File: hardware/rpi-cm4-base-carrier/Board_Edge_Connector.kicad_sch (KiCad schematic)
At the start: 3 parts, among them J2 ERM8-040-01-X-D-EM2-L-XX, J8 Conn_02x10_Odd_Even, U2 74LVC1G07SE-7

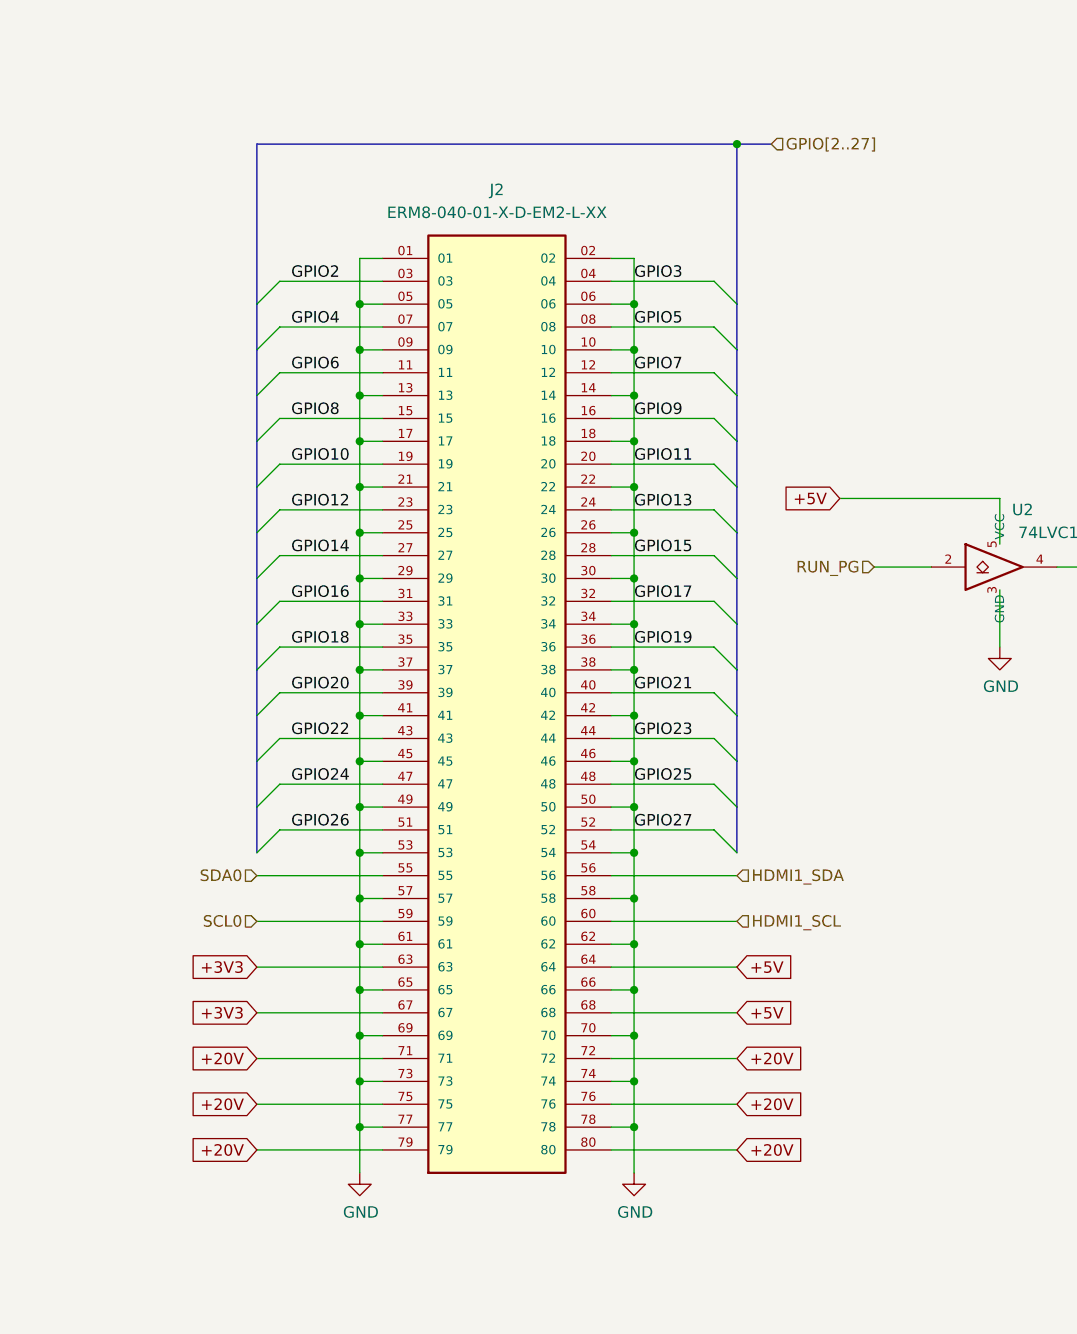
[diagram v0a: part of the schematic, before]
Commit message: board edge connector mostly connected
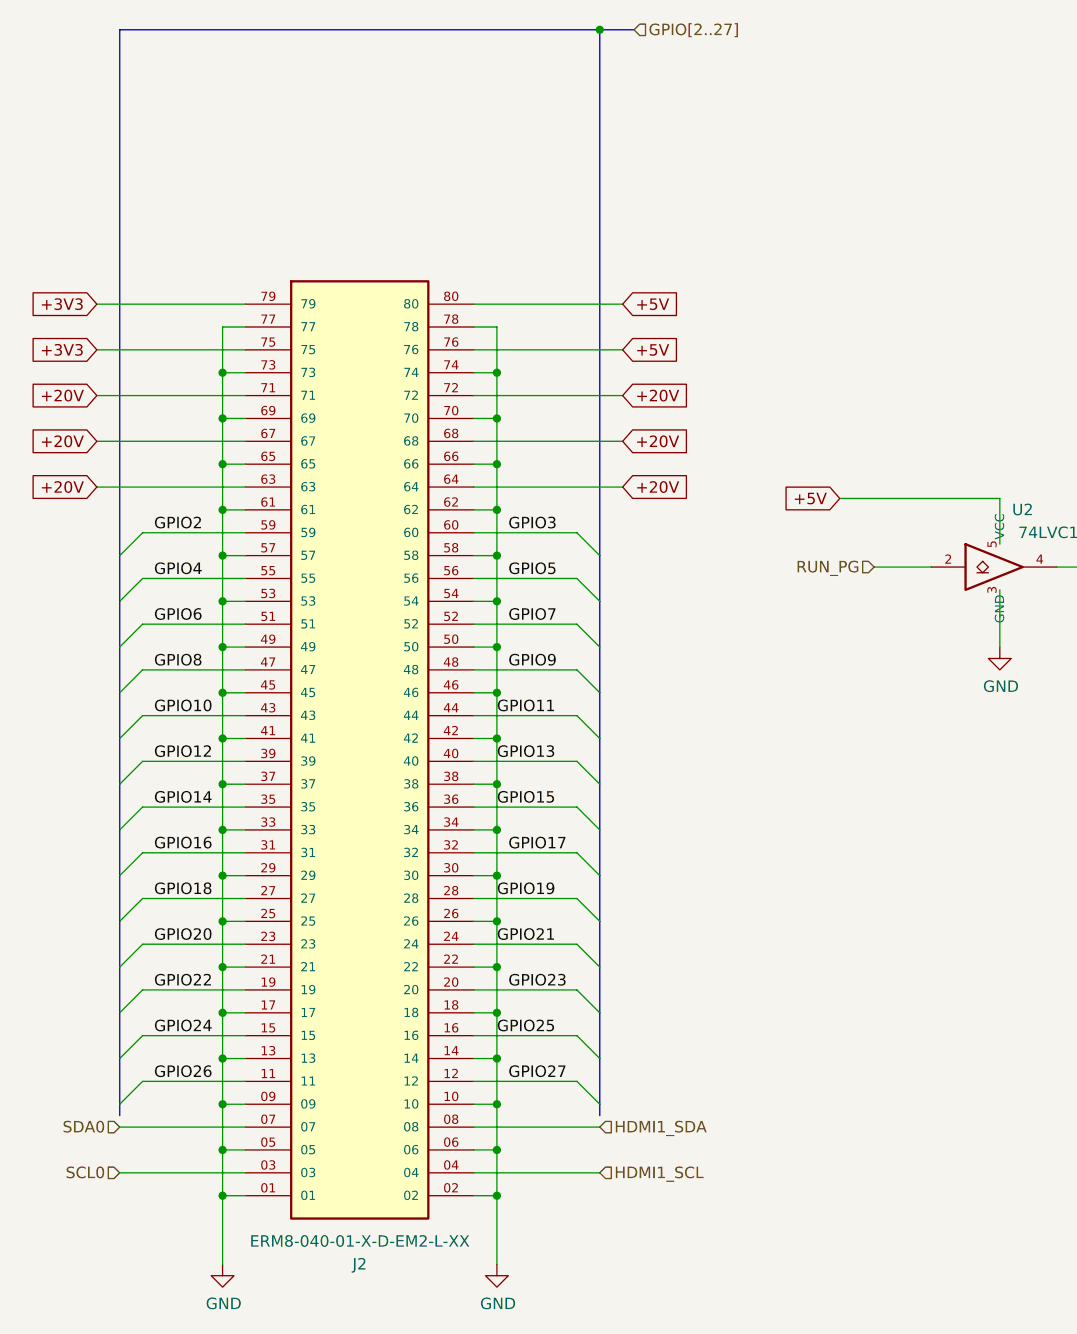
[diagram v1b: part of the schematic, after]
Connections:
- net +20V: now also J2.63, J2.64, J2.67, J2.68; no longer J2.75, J2.76, J2.79, J2.80
- net +3V3: now also J2.75, J2.79; no longer J2.63, J2.67
- net +5V: now also J2.76, J2.80; no longer J2.64, J2.68
- net GND: no longer J2.04, J2.08, J2.12, J2.20, J2.32, J2.48, J2.52, J8.1 (Pin_1), J8.2 (Pin_2)
- net GPIO10: now also J2.43; no longer J2.19
- net GPIO12: now also J2.39; no longer J2.23
- net GPIO14: now also J2.35; no longer J2.27
- net GPIO18: now also J2.27; no longer J2.35
- net GPIO2: now also J2.59; no longer J2.03
- net GPIO20: now also J2.23; no longer J2.39
- net GPIO22: now also J2.19; no longer J2.43
- net GPIO24: now also J2.15; no longer J2.47
- net GPIO26: now also J2.11; no longer J2.51
- net GPIO4: now also J2.55; no longer J2.07
- net GPIO6: now also J2.51; no longer J2.11
- net GPIO8: now also J2.47; no longer J2.15
- net HDMI1_SCL: now also J2.04; no longer J2.60
- net HDMI1_SDA: now also J2.08; no longer J2.56
- net SCL0: now also J2.03; no longer J2.59
- net SDA0: now also J2.07; no longer J2.55
- new net GPIO17: J2.32
- new net GPIO23: J2.20
- new net GPIO27: J2.12
- new net GPIO3: J2.60
- new net GPIO5: J2.56
- new net GPIO7: J2.52, J8.2 (Pin_2)
- new net GPIO9: J2.48, J8.1 (Pin_1)

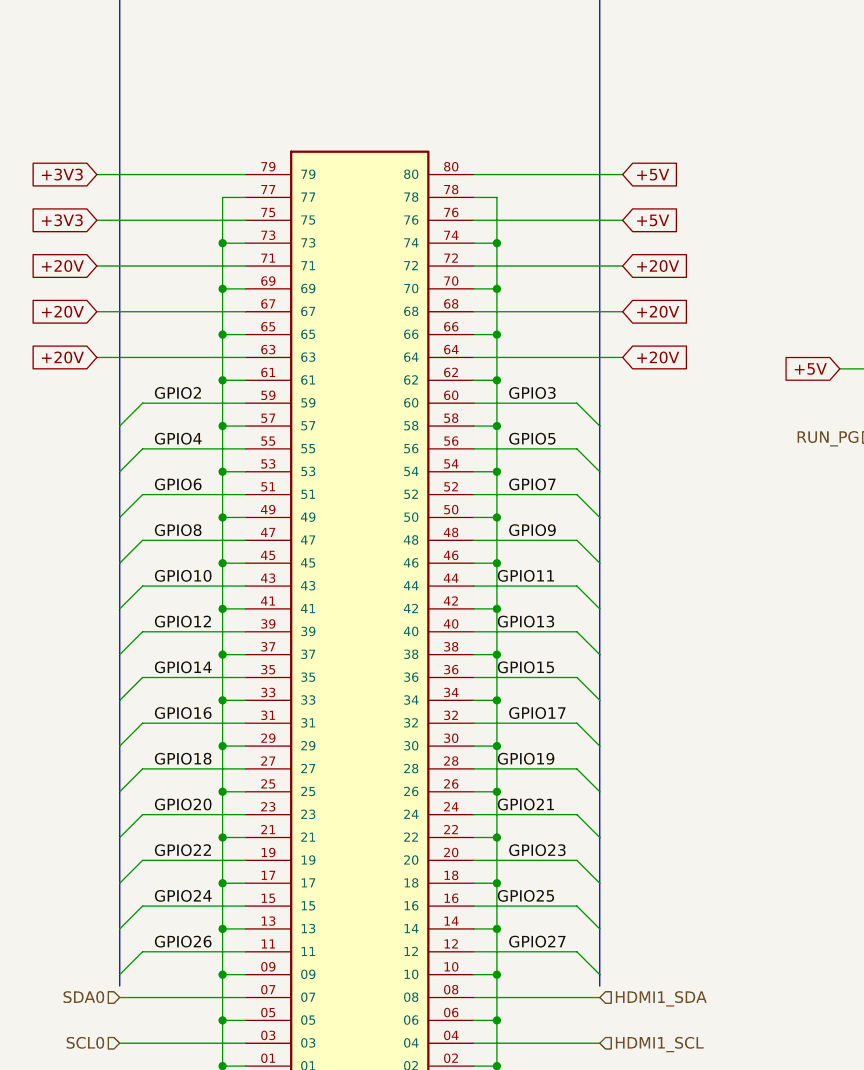
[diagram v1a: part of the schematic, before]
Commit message: good routing and power plane progress, just some final plane progress remaining
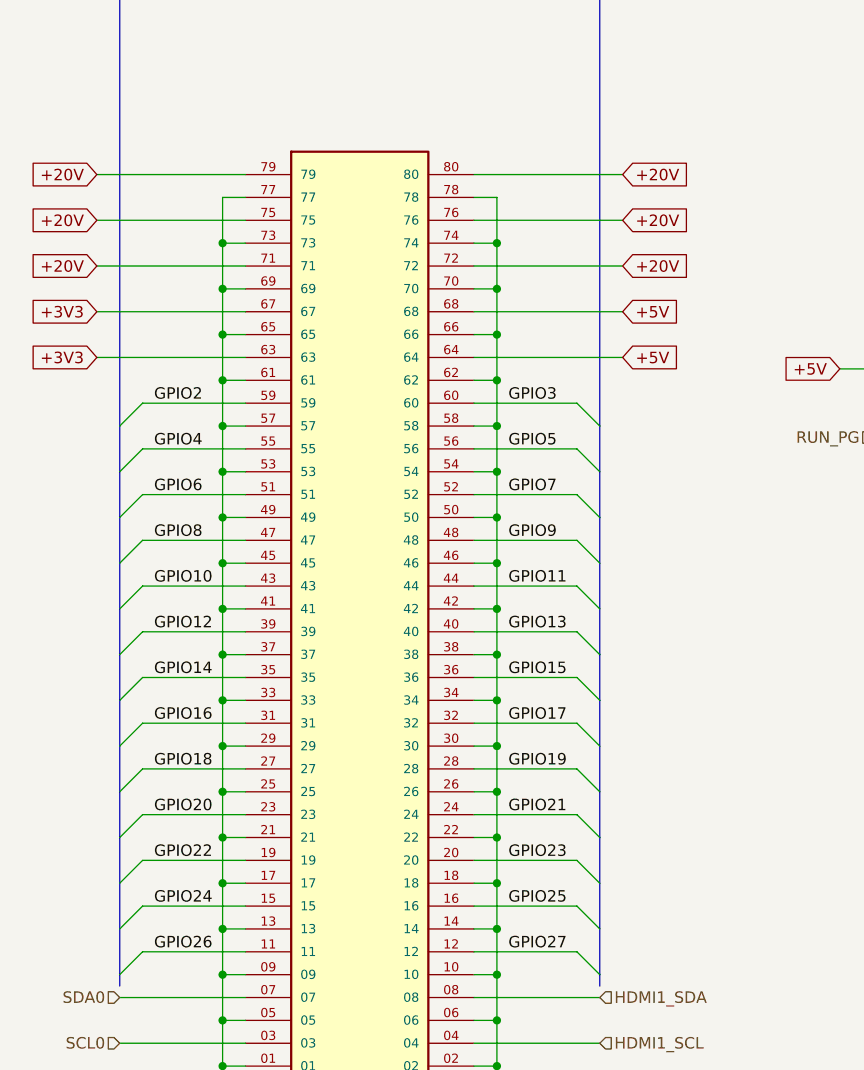
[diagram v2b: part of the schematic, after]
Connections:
- net +20V: now also J2.75, J2.76, J2.79, J2.80; no longer J2.63, J2.64, J2.67, J2.68
- net +3V3: now also J2.63, J2.67; no longer J2.75, J2.79
- net +5V: now also J2.64, J2.68; no longer J2.76, J2.80
- net GND: no longer J2.16, J2.24, J2.28, J2.36, J2.40, J2.44, J8.5 (Pin_5), J8.6 (Pin_6)
- new net GPIO11: J2.44, J8.6 (Pin_6)
- new net GPIO13: J2.40
- new net GPIO15: J2.36, J8.5 (Pin_5)
- new net GPIO19: J2.28
- new net GPIO21: J2.24
- new net GPIO25: J2.16

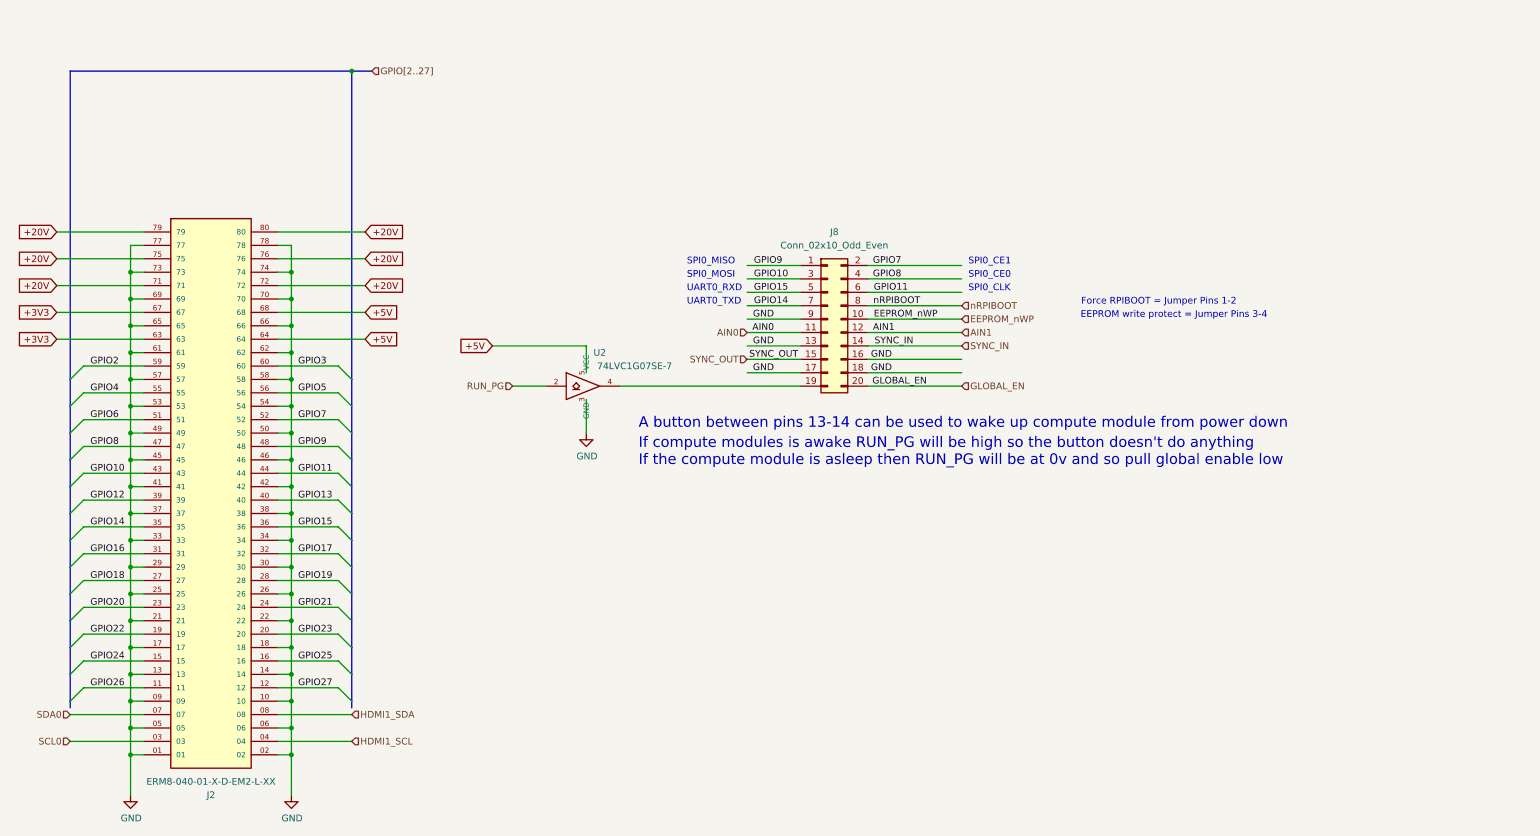
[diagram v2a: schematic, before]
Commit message: convert IC refs to U refs and re-annotate, add fiducials and extra via stitching to layout
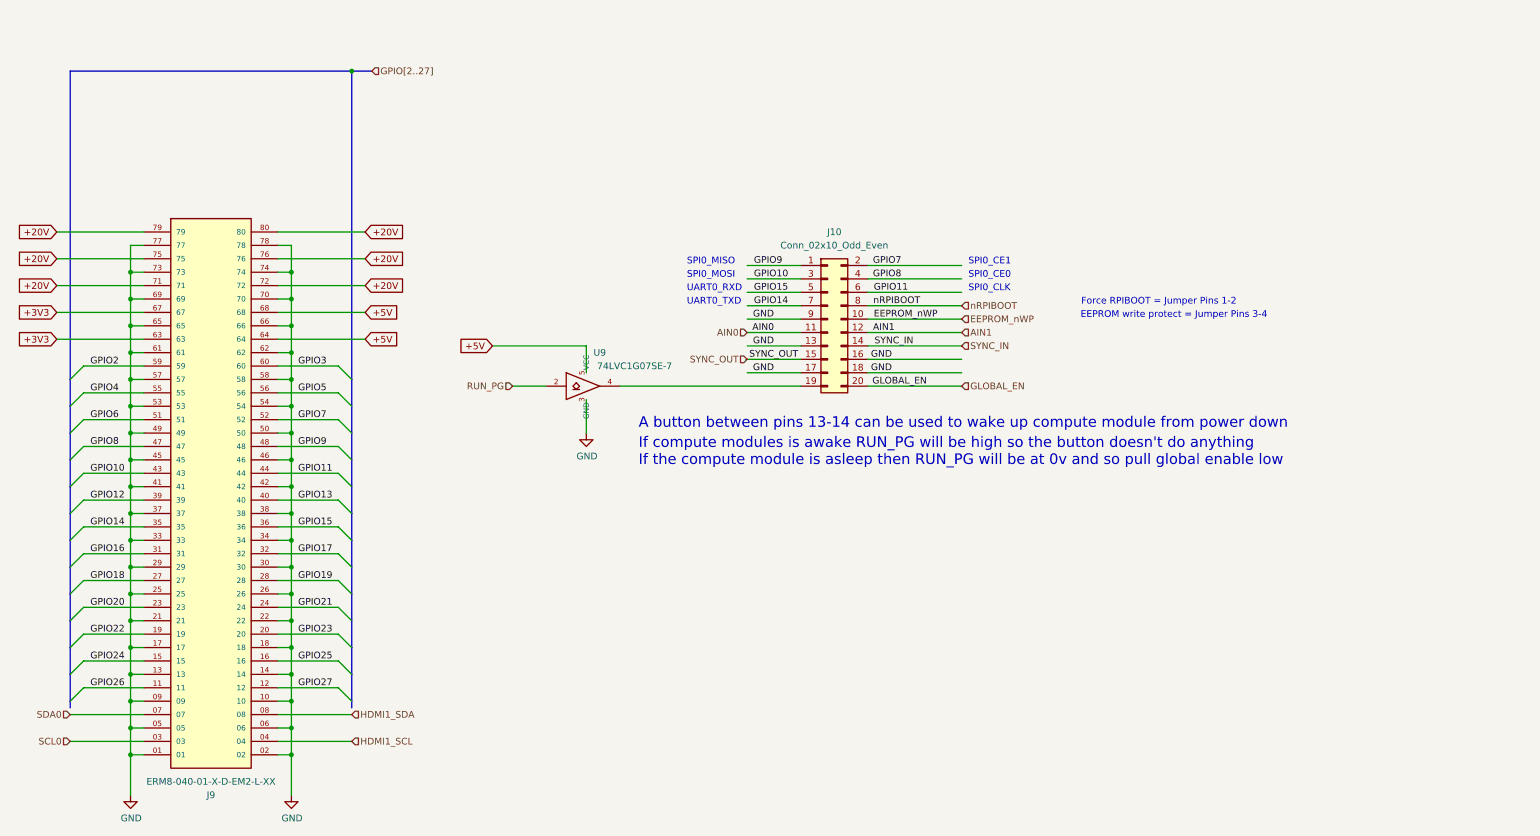
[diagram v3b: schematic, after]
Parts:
- renumbered J8 to J10, J2 to J9, U2 to U9
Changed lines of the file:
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@@
   (symbol (lib_id "Connector_Generic:Conn_02x10_Odd_Even") (at 168.91 78.74 0) (unit 1)
     (in_bom yes) (on_board yes) (dnp no) (fields_autoplaced)
-    (property "Reference" "J8" (at 170.18 62.23 0)
+    (property "Reference" "J10" (at 170.18 62.23 0)
       (effects (font (size 1.27 1.27)))
     )
@@
       (project "rpi-cm4-base-carrier"
         (path "/92c58705-ecb0-498b-b561-44a3f0daad57/7444e048-4ed9-432f-b4ba-4c016f1c7845"
-          (reference "J8") (unit 1)
+          (reference "J10") (unit 1)
         )
       )
@@
   (symbol (lib_id "CM4IO:74LVC1G07_copy") (at 123.19 91.44 0) (unit 1)
     (in_bom yes) (on_board yes) (dnp no)
-    (property "Reference" "U2" (at 125.73 85.09 0)
+    (property "Reference" "U9" (at 125.73 85.09 0)
       (effects (font (size 1.27 1.27)))
     )
@@
       (project "rpi-cm4-base-carrier"
         (path "/92c58705-ecb0-498b-b561-44a3f0daad57/7444e048-4ed9-432f-b4ba-4c016f1c7845"
-          (reference "U2") (unit 1)
+          (reference "U9") (unit 1)
         )
       )
@@
         )
         (path "/92c58705-ecb0-498b-b561-44a3f0daad57/7444e048-4ed9-432f-b4ba-4c016f1c7845"
-          (reference "#PWR056") (unit 1)
+          (reference "#PWR064") (unit 1)
         )
       )
@@
   (symbol (lib_id "ERM8-040-01-X-D-EM2-L-XX:ERM8-040-01-X-D-EM2-L-XX") (at 52.07 113.03 0) (mirror x) (unit 1)
     (in_bom yes) (on_board yes) (dnp no)
-    (property "Reference" "J2" (at 52.07 168.91 0)
+    (property "Reference" "J9" (at 52.07 168.91 0)
       (effects (font (size 1.27 1.27)))
     )
@@
       (project "rpi-cm4-base-carrier"
         (path "/92c58705-ecb0-498b-b561-44a3f0daad57/7444e048-4ed9-432f-b4ba-4c016f1c7845"
-          (reference "J2") (unit 1)
+          (reference "J9") (unit 1)
         )
       )
@@
         )
         (path "/92c58705-ecb0-498b-b561-44a3f0daad57/7444e048-4ed9-432f-b4ba-4c016f1c7845"
-          (reference "#PWR012") (unit 1)
+          (reference "#PWR065") (unit 1)
         )
       )
@@
   (symbol (lib_id "power:GND") (at 123.19 100.33 0) (unit 1)
     (in_bom yes) (on_board yes) (dnp no)
-    (property "Reference" "#PWR057" (at 123.19 106.68 0)
+    (property "Reference" "#PWR066" (at 123.19 106.68 0)
       (effects (font (size 1.27 1.27)) hide)
     )
@@
       (project "rpi-cm4-base-carrier"
         (path "/92c58705-ecb0-498b-b561-44a3f0daad57/7444e048-4ed9-432f-b4ba-4c016f1c7845"
-          (reference "#PWR057") (unit 1)
-        )
-      )
+          (reference "#PWR066") (unit 1)
+        )
+      )

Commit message: design files exported ready for manufacture, LCSC part numbers added throughout the library
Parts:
- J10: LCSC Part # (none) -> C5372868; LCSC Part Number (none) -> C5372868
- J9: LCSC Part # (none) -> Non Stock; LCSC Part Number (none) -> Non Stock
- U9: LCSC Part # (none) -> C2675596; LCSC Part Number (none) -> C2675596
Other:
- title: (none) -> Raspberry Pi Compute Module 4 Control Node
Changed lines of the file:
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@@
 (kicad_sch (version 20230121) (generator eeschema)
   (paper "A4")
+  (title_block
+    (title "Raspberry Pi Compute Module 4 Control Node")
+    (date "2024-02-04")
+    (comment 2 "creativecommons.org/licenses/by-sa/4.0/")
+    (comment 3 "License: CC BY-SA 4.0")
+    (comment 4 "Author: Sam Earnshaw")
+  )
   (junction (at 67.31 140.97) (diameter 0) (color 0 0 0 0)
   )
@@
     )
     (property "Datasheet" "~" (at 168.91 78.74 0)
+      (effects (font (size 1.27 1.27)) hide)
+    )
+    (property "LCSC Part Number" "C5372868" (at 168.91 78.74 0)
+      (effects (font (size 1.27 1.27)) hide)
+    )
+    (property "LCSC Part #" "C5372868" (at 168.91 78.74 0)
       (effects (font (size 1.27 1.27)) hide)
     )
@@
       (effects (font (size 1.27 1.27)) hide)
     )
+    (property "LCSC Part Number" "C2675596" (at 123.19 91.44 0)
+      (effects (font (size 1.27 1.27)) hide)
+    )
+    (property "LCSC Part #" "C2675596" (at 123.19 91.44 0)
+      (effects (font (size 1.27 1.27)) hide)
+    )
     (pin "2")
     (pin "3")
@@
       (effects (font (size 1.27 1.27)) (justify bottom) hide)
     )
+    (property "LCSC Part Number" "Non Stock" (at 52.07 113.03 0)
+      (effects (font (size 1.27 1.27)) hide)
+    )
+    (property "LCSC Part #" "Non Stock" (at 52.07 113.03 0)
+      (effects (font (size 1.27 1.27)) hide)
+    )
     (pin "44")
